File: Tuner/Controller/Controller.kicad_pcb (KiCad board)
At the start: 2 copper layers, 96.8 x 99.3 mm, 173 parts, among them J1 Conn_02x05_Odd_Even, J10 Conn_01x05, J12 Conn_01x02, J15 Conn_01x02, J16 Conn_01x06, J18 Conn_01x01, J19 Conn_01x01, J2 Conn_02x05_Odd_Even, J20 Conn_01x01, J21 Conn_01x01, J26 Conn_01x02, J27 Conn_01x02, J28 Conn_01x02, J3 Conn_02x05_Odd_Even, J30 Conn_01x02, J4 Conn_02x05_Odd_Even, J5 Conn_02x05_Odd_Even, J6 Conn_01x02, J7 Conn_01x02, J8 Conn_01x06, Q1 2N3904, Q2 2N3904, Q3 2N3904, Q4 2N3904, Q5 2N3904, Q6 2N3904, Q7 2N3904, Q8 2N3904, U1 74LS393, U2 74HC14, U3 74HC86, U4 LM350_TO220

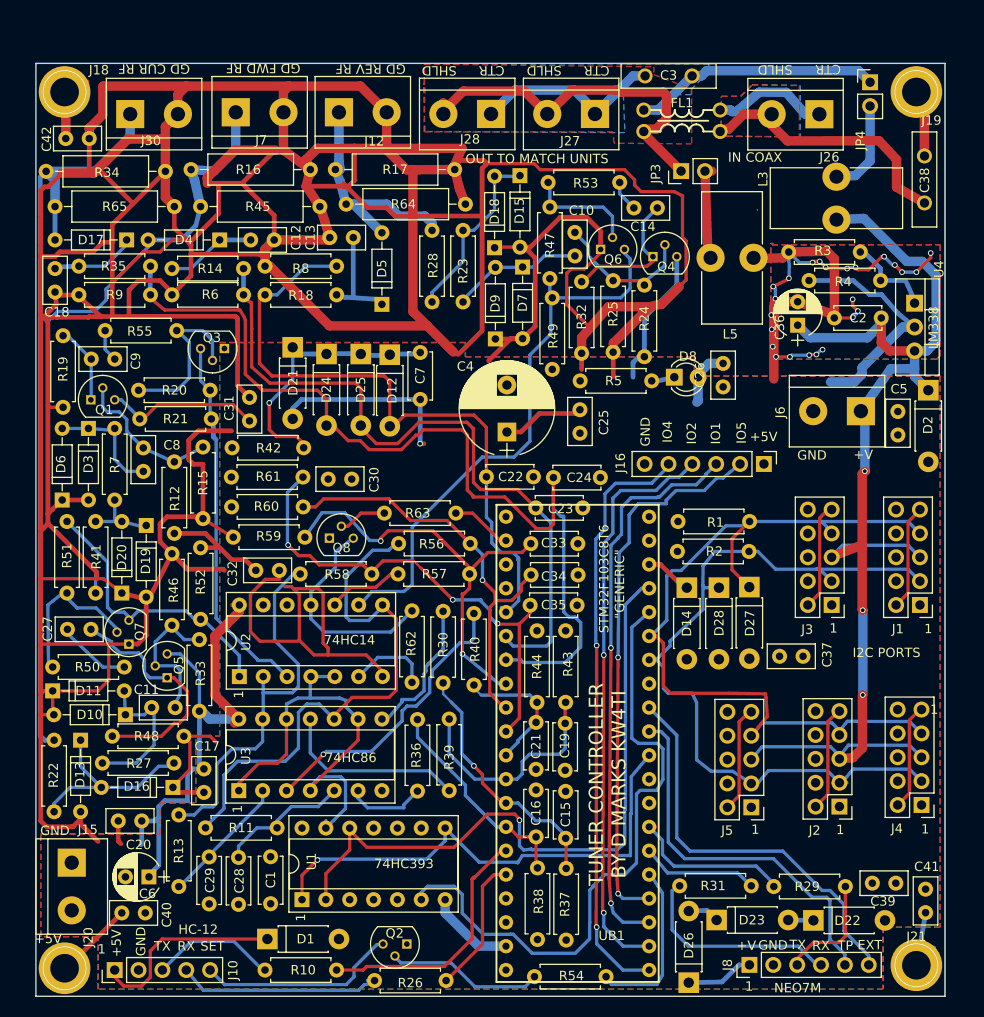
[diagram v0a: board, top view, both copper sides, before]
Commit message: Added BNC and screw terminal combo pads
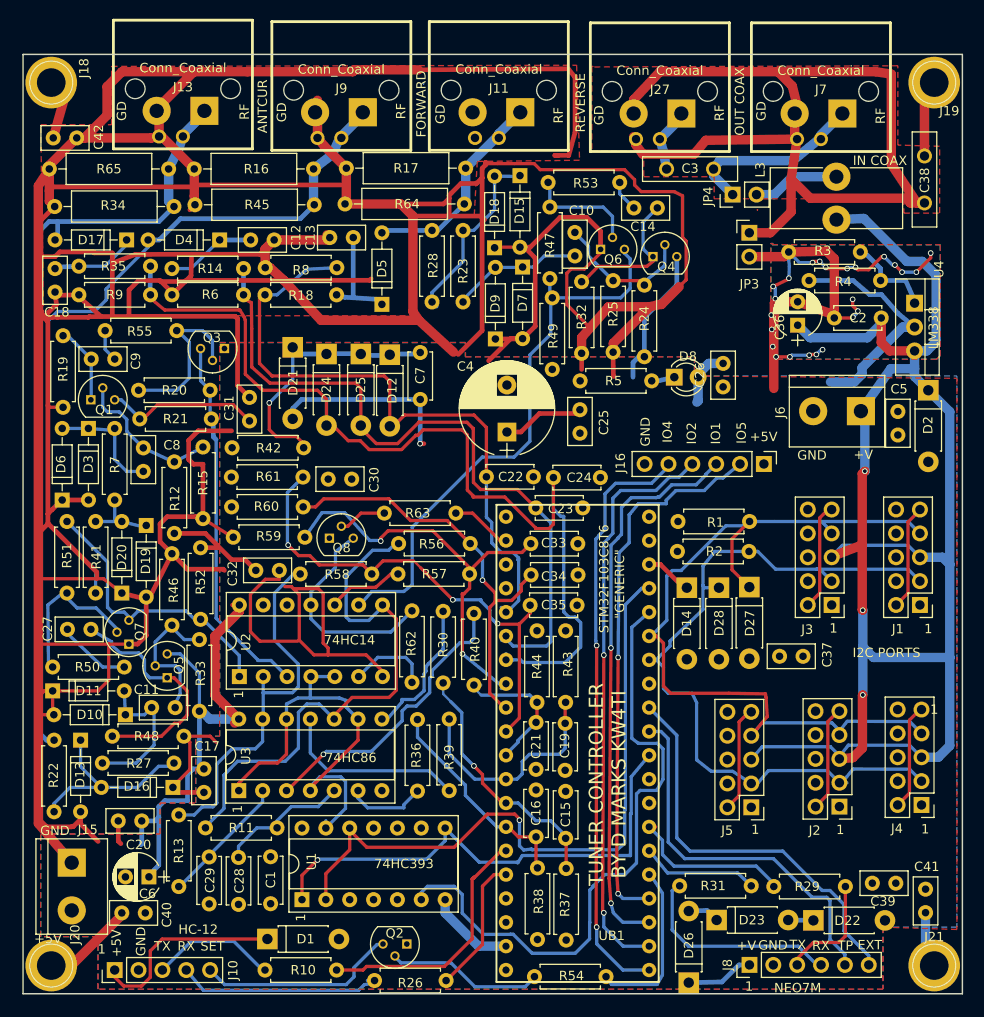
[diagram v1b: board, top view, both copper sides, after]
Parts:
- removed FL1: Choke, Controller:GenericCMCL
- removed J12, J26, J28, J30: Conn_01x02, Connectors_Terminal_Blocks:TerminalBlock_bornier-2_P5.08mm
- removed L5: 100 uH, Inductors_THT:L_Toroid_Vertical_L14.0mm_W6.3mm_P4.57mm_Pulse_A
- added J11: Conn_Coaxial, Controller:bnc_90_1-1337543-0_pad_combo, F.Cu at (104.6, 24.5)
- added J13: Conn_Coaxial, Controller:bnc_90_1-1337543-0_pad_combo, F.Cu at (71.0, 24.4)
- added J9: Conn_Coaxial, Controller:bnc_90_1-1337543-0_pad_combo, F.Cu at (87.9, 24.5)
- J27, J7: value Conn_01x02 -> Conn_Coaxial; footprint Connectors_Terminal_Blocks:TerminalBlock_bornier-2_P5.08mm -> Controller:bnc_90_1-1337543-0_pad_combo
- R16, R17, R34, R45, R64, R65: value 33R -> 133R
- moved J7 63.0 mm to (138.9, 24.6), turned to 180 degrees
- moved JP4 18.9 mm to (129.5, 42.9), turned to 90 degrees
- moved R34 14.1 mm to (70.1, 44.2), turned to 180 degrees
- moved R17 13.9 mm to (101.1, 40.1), turned to 180 degrees
- moved R16 13.0 mm to (84.9, 40.2), turned to 180 degrees
- moved R65 12.7 mm to (69.5, 40.2), turned to 180 degrees
- moved R64 12.6 mm to (101.0, 43.9), turned to 180 degrees
- moved R45 12.1 mm to (85.0, 44.0), turned to 180 degrees
- moved J27 11.9 mm to (121.8, 24.6)
- moved C3 10.2 mm to (127.5, 40.2)
- moved JP3 9.79 mm to (131.3, 47.0), turned to 0 degrees
- moved J19 2.15 mm to (151.0, 31.0)
- moved J21 1.90 mm to (151.0, 125.0)
- moved J18 1.74 mm to (57.0, 31.0)
- moved J20 1.45 mm to (57.0, 125.0)
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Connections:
- J27 pad 2: Net-(FL1-Pad4) -> Net-(C38-Pad1)
- J7 pad 1: XFwd -> Net-(C3-Pad1)
- J7 pad 2: GND -> Net-(C38-Pad1)
- JP3 pad 1: Net-(FL1-Pad4) -> Net-(C38-Pad1)
- JP3 pad 2: Net-(JP3-Pad2) -> GND
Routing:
- net Net-(C38-Pad1): track 30.3 -> 103.5 mm
- net UPWR: track 127.7 -> 183.3 mm
- net GND: track 833.7 -> 888.7 mm
- net Net-(FL1-Pad4): track 42.0 -> 0.00 mm
- net Net-(FL1-Pad1): track 15.5 -> 0.00 mm
- net Net-(C3-Pad2): track 21.5 -> 6.95 mm
- net Net-(JP3-Pad2): track 10.1 -> 0.00 mm
- net XFwd: track 68.1 -> 78.1 mm
- net Net-(C3-Pad1): track 26.9 -> 19.9 mm
- net XRev: track 25.7 -> 22.6 mm
- net XCur: track 82.9 -> 84.9 mm
- net Net-(C40-Pad1): track 8.50 -> 10.2 mm
- net Net-(C42-Pad1): track 6.56 -> 5.13 mm
- net Net-(JP4-Pad2): track 10.5 -> 9.30 mm
- removed copper zone on B.Cu, net Net-(FL1-Pad1)
- removed copper zone on F.Cu, net Net-(FL1-Pad4)
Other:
- board size 96.8 x 99.3 mm -> 100 x 100 mm
- board text added: "ANTCUR"
- board text added: "FORWARD"
- board text added: "GD"
- board text added: "OUT COAX"
- board text added: "REVERSE"
- board text added: "RF"
- board text removed: "CTR"
- board text removed: "GD CUR RF"
- board text removed: "GD FWD RF"
- board text removed: "GD REV RF"
- board text removed: "OUT TO MATCH UNITS"
- board text removed: "SHLD"

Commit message: Modified connectors on Reversible boards
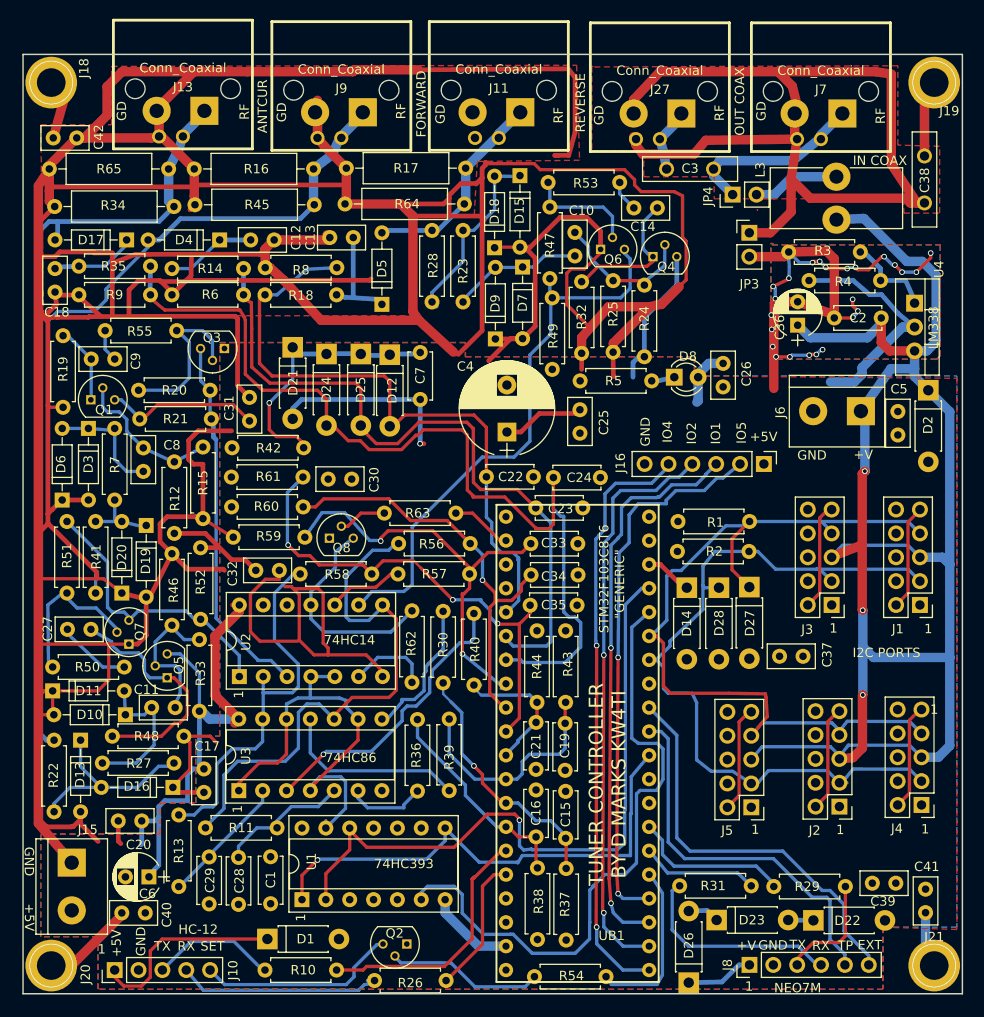
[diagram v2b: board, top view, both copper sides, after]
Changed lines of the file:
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@@
   )
   (setup
-    (last_trace_width 1)
+    (last_trace_width 0.25)
     (user_trace_width 0.35)
     (user_trace_width 0.5)
@@
     (descr "C, Disc series, Radial, pin pitch=2.50mm, , diameter*width=5*2.5mm^2, Capacitor, http://cdn-reichelt.de/documents/datenblatt/B300/DS_KERKO_TC.pdf")
     (tags "C Disc series Radial pin pitch 2.50mm  diameter 5mm width 2.5mm Capacitor")
-    (fp_text reference C26 (at 1.2446 2.4638 270) (layer F.SilkS)
+    (fp_text reference C26 (at 1.1049 -2.4892 270) (layer F.SilkS)
       (effects (font (size 1 1) (thickness 0.15)))
     )
@@
     (descr "module 1 pin (ou trou mecanique de percage)")
     (tags DEV)
-    (fp_text reference J20 (at 2.54 -3.302 90) (layer F.SilkS)
+    (fp_text reference J20 (at 3.6552 0.9332 90) (layer F.SilkS)
       (effects (font (size 1 1) (thickness 0.15)))
     )
@@
     (effects (font (size 1 1) (thickness 0.15)))
   )
-  (gr_text GND (at 57.3913 110.6424) (layer F.SilkS)
+  (gr_text GND (at 54.6354 113.919 270) (layer F.SilkS)
     (effects (font (size 1 1) (thickness 0.15)))
   )
-  (gr_text +5V (at 56.6547 122.1486) (layer F.SilkS)
+  (gr_text +5V (at 54.6608 119.8626 270) (layer F.SilkS)
     (effects (font (size 1 1) (thickness 0.15)))
   )

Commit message: A few tweaks
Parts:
- removed D22, D23, D26: 1N4001, Diodes_THT:D_DO-41_SOD81_P7.62mm_Horizontal
- added C43: 10 nF, Capacitors_THT:C_Disc_D5.0mm_W2.5mm_P2.50mm, F.Cu at (100.6, 47.0)
- added C44: 10 nF, Capacitors_THT:C_Disc_D5.0mm_W2.5mm_P2.50mm, F.Cu at (57.5, 53.6)
- added C45: 10 nF, Capacitors_THT:C_Disc_D5.0mm_W2.5mm_P2.50mm, F.Cu at (58.6, 57.7)
- moved C26 61.3 mm to (147.1, 119.3), turned to 90 degrees
- moved C39 22.0 mm to (126.6, 124.7)
- moved R19 7.76 mm to (65.6, 60.5), turned to 180 degrees
- moved C9 6.71 mm to (70.5, 60.6)
- moved R8 3.66 mm to (91.1, 50.8)
- moved R18 3.57 mm to (90.9, 53.8)
- moved R6 3.56 mm to (81.0, 53.7)
- moved R9 3.30 mm to (70.9, 53.7)
- moved R35 3.30 mm to (63.2, 50.7)
- moved R14 3.30 mm to (73.2, 50.8)
- moved C18 3.19 mm to (60.6, 51.1)
- moved R23 2.54 mm to (101.0, 49.3)
- moved R28 2.50 mm to (98.2, 49.1)
- moved J15 1.97 mm to (59.2, 112.1)
- moved Q3 1.94 mm to (77.4, 59.5)
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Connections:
- J8 pad 1: Net-(D26-Pad1) -> +5V
- R22 pad 1: XCur -> Net-(C44-Pad1)
- R28 pad 1: XRev -> Net-(C43-Pad1)
- R41 pad 1: XFwd -> Net-(C45-Pad1)
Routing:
- net XCur: track 84.9 -> 29.0 mm
- net Net-(C44-Pad1): track 0.00 -> 50.6 mm
- net XFwd: track 78.1 -> 45.7 mm
- net Net-(C45-Pad1): track 0.00 -> 31.7 mm
- net GND: track 888.7 -> 917.0 mm
- net +5V: track 199.7 -> 224.9 mm
- net Net-(D26-Pad1): track 7.22 -> 0.00 mm
- net Net-(C43-Pad1): track 0.00 -> 3.93 mm
- net Net-(C9-Pad1): track 3.45 -> 7.14 mm
- net Net-(D23-Pad1): track 3.39 -> 0.00 mm
- net Net-(D15-Pad1): track 19.8 -> 22.6 mm
- net Net-(D22-Pad1): track 2.68 -> 0.00 mm
- net VCur: track 102.8 -> 100.2 mm
- net Net-(C10-Pad1): track 14.7 -> 16.3 mm
- net Net-(C9-Pad2): track 8.39 -> 9.97 mm
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
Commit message: Actually tuning code now!
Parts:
- moved R11 0.06 mm to (73.4, 110.3)
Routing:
- net GND: track 917.0 -> 1016.3 mm
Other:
- board text added: "NEO7M/PROG"
- board text removed: "NEO7M"

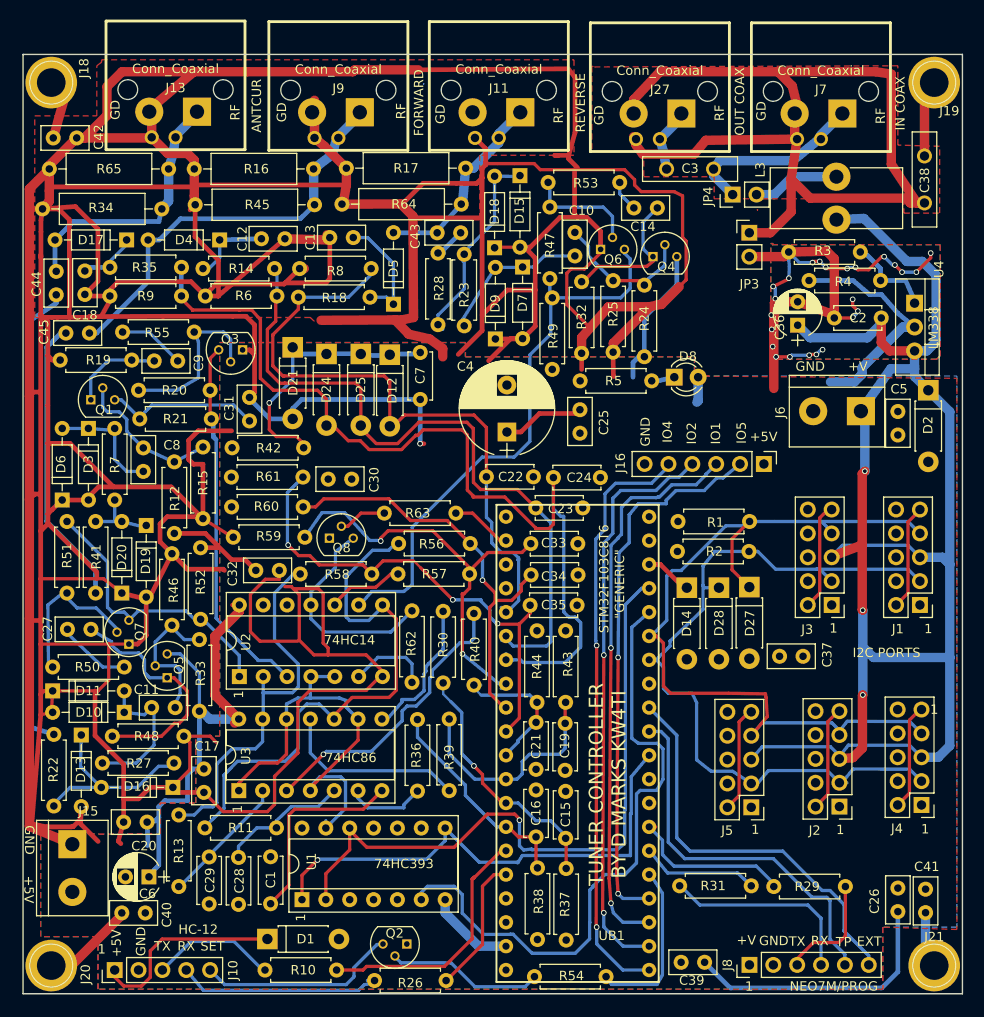
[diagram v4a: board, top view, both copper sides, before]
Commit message: Put level shifters into controller
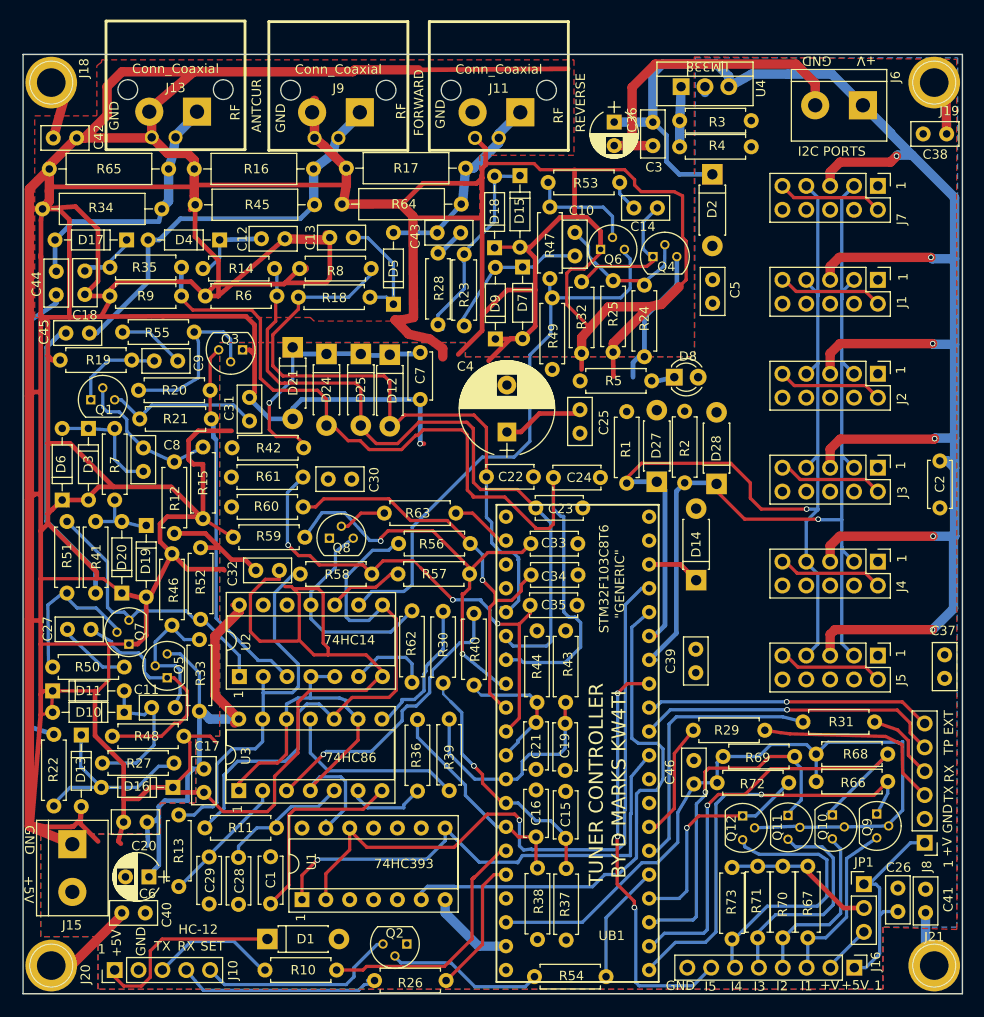
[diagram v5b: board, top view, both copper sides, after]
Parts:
- removed J27: Conn_Coaxial, Controller:bnc_90_1-1337543-0_pad_combo
- removed JP3, JP4: Jumper, Pin_Headers:Pin_Header_Straight_1x02_Pitch2.54mm
- removed L3: 100 uH, Inductors_THT:L_Toroid_Vertical_L14.0mm_W6.3mm_P4.57mm_Pulse_A
- added C46: 100 nF, Capacitors_THT:C_Disc_D5.0mm_W2.5mm_P2.50mm, F.Cu at (125.4, 105.7)
- added JP1: Jumper_NC_Dual, Pin_Headers:Pin_Header_Straight_1x03_Pitch2.54mm, F.Cu at (143.5, 116.3)
- added Q10: 2N7000, TO_SOT_Packages_THT:TO-92_Molded_Narrow, F.Cu at (140.2, 109.0)
- added Q11: 2N7000, TO_SOT_Packages_THT:TO-92_Molded_Narrow, F.Cu at (135.4, 109.0)
- added Q12: 2N7000, TO_SOT_Packages_THT:TO-92_Molded_Narrow, F.Cu at (130.6, 109.1)
- added Q9: 2N7000, TO_SOT_Packages_THT:TO-92_Molded_Narrow, F.Cu at (144.9, 108.9)
- added R66: 10k, Resistors_THT:R_Axial_DIN0207_L6.3mm_D2.5mm_P7.62mm_Horizontal, F.Cu at (146.1, 105.4)
- added R67: 10k, Resistors_THT:R_Axial_DIN0207_L6.3mm_D2.5mm_P7.62mm_Horizontal, F.Cu at (137.5, 122.0)
- added R68: 10k, Resistors_THT:R_Axial_DIN0207_L6.3mm_D2.5mm_P7.62mm_Horizontal, F.Cu at (146.1, 102.5)
- added R69: 10k, Resistors_THT:R_Axial_DIN0207_L6.3mm_D2.5mm_P7.62mm_Horizontal, F.Cu at (136.1, 102.7)
- added R70: 10k, Resistors_THT:R_Axial_DIN0207_L6.3mm_D2.5mm_P7.62mm_Horizontal, F.Cu at (134.9, 122.0)
- added R71: 10k, Resistors_THT:R_Axial_DIN0207_L6.3mm_D2.5mm_P7.62mm_Horizontal, F.Cu at (132.2, 122.0)
- added R72: 10k, Resistors_THT:R_Axial_DIN0207_L6.3mm_D2.5mm_P7.62mm_Horizontal, F.Cu at (135.5, 105.5)
- added R73: 10k, Resistors_THT:R_Axial_DIN0207_L6.3mm_D2.5mm_P7.62mm_Horizontal, F.Cu at (129.5, 122.2)
- C3, C38: footprint Capacitors_THT:C_Disc_D10.0mm_W2.5mm_P5.00mm -> Capacitors_THT:C_Disc_D5.0mm_W2.5mm_P2.50mm
- J16: value Conn_01x06 -> Conn_01x08; footprint Pin_Headers:Pin_Header_Straight_1x06_Pitch2.54mm -> Pin_Headers:Pin_Header_Straight_1x08_Pitch2.54mm
- J7: value Conn_Coaxial -> Conn_02x05_Odd_Even; footprint Controller:bnc_90_1-1337543-0_pad_combo -> Pin_Headers:Pin_Header_Straight_2x05_Pitch2.54mm
- moved J16 54.5 mm to (142.5, 125.2)
- moved J2 46.3 mm to (145.0, 62.0), turned to 270 degrees
- moved J1 34.9 mm to (145.0, 52.0), turned to 270 degrees
- moved U4 33.9 mm to (124.1, 31.4), turned to 0 degrees
- moved J6 32.6 mm to (143.4, 33.4)
- moved D2 32.5 mm to (127.4, 40.8)
- moved C39 30.8 mm to (125.6, 93.8), turned to 90 degrees
- moved C36 29.1 mm to (116.9, 35.2), turned to 270 degrees
- moved R31 27.1 mm to (144.7, 99.1), turned to 180 degrees
- moved J4 26.3 mm to (145.0, 82.0), turned to 270 degrees
- moved C5 24.2 mm to (127.4, 54.5)
- moved C2 23.1 mm to (151.6, 76.3), turned to 90 degrees
- moved J8 22.7 mm to (150.0, 111.9), turned to 180 degrees
- moved J5 21.0 mm to (145.0, 92.0), turned to 270 degrees
- moved R29 18.7 mm to (133.0, 99.9)
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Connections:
- C3 pad 1: Net-(C3-Pad1) -> GND
- C3 pad 2: Net-(C3-Pad2) -> UPWR
- C38 pad 2: Net-(C38-Pad2) -> GND
- J16 pad 2: IO5 -> Net-(J16-Pad2)
- J16 pad 3: IO1 -> Net-(J16-Pad3)
- J16 pad 4: IO2 -> Net-(J16-Pad4)
- J16 pad 5: IO4 -> Net-(J16-Pad5)
- J16 pad 6: GND -> Net-(J16-Pad6)
- J19 pad 1: Net-(C38-Pad2) -> Net-(C38-Pad1)
- J7 pad 1: Net-(C3-Pad1) -> GND
- J7 pad 2: Net-(C38-Pad1) -> +5V
- UB1 pad 25: IO4 -> IO1
- UB1 pad 27: IO1 -> IO3
- UB1 pad 28: IO5 -> IO4
- UB1 pad 41: (no net) -> IO5
- UB1 pad 70: (no net) -> +3V3
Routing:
- net Net-(C38-Pad1): track 103.5 -> 9.11 mm
- net +3V3: track 0.00 -> 82.8 mm
- net GND: track 1016.3 -> 956.7 mm, vias 25 -> 1
- net IO4: track 63.8 -> 24.4 mm, vias 2 -> 1
- net IO3: track 0.00 -> 38.7 mm, vias 0 -> 1
- net Net-(J16-Pad6): track 0.00 -> 29.0 mm
- net +5V: track 225.0 -> 199.9 mm
- net Net-(J16-Pad5): track 0.00 -> 24.3 mm
- net Net-(C3-Pad1): track 19.9 -> 0.00 mm
- net Net-(J16-Pad4): track 0.00 -> 19.6 mm
- net Net-(J16-Pad3): track 0.00 -> 18.6 mm
- net Net-(R31-Pad2): track 12.8 -> 29.8 mm
- net Net-(JP1-Pad2): track 0.00 -> 16.5 mm
- net IO5: track 59.2 -> 44.4 mm, vias 2 -> 3
- net IO1: track 59.9 -> 45.6 mm, vias 2 -> 1
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- removed copper zone on F.Cu, net +5V
- removed copper zone on B.Cu, net GND
- removed copper zone on B.Cu, net Net-(C3-Pad2)
- removed copper zone on F.Cu, net Net-(C38-Pad1)
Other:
- board text added: "I1"
- board text added: "I2"
- board text added: "I3"
- board text added: "I4"
- board text added: "I5"
- board text removed: "GD"
- board text removed: "IN COAX"
- board text removed: "IO1"
- board text removed: "IO2"
- board text removed: "IO4"
- board text removed: "IO5"
- board text removed: "NEO7M/PROG"
- board text removed: "OUT COAX"
